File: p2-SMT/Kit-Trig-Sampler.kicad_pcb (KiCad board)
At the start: 2 copper layers, 78 x 109.2 mm, 81 parts, among them J1 START_CV, J10 AUDIO_INR, J11 AUDIO_OUTL, J13 BANK_CV, J14 Eurorack_Power_10pin_Unshroud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, J2 LENGTH_CV, J3 SAMP_CV, J4 PITCH CV, J5 REV_TRIG, J6 PLAY_TRIG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

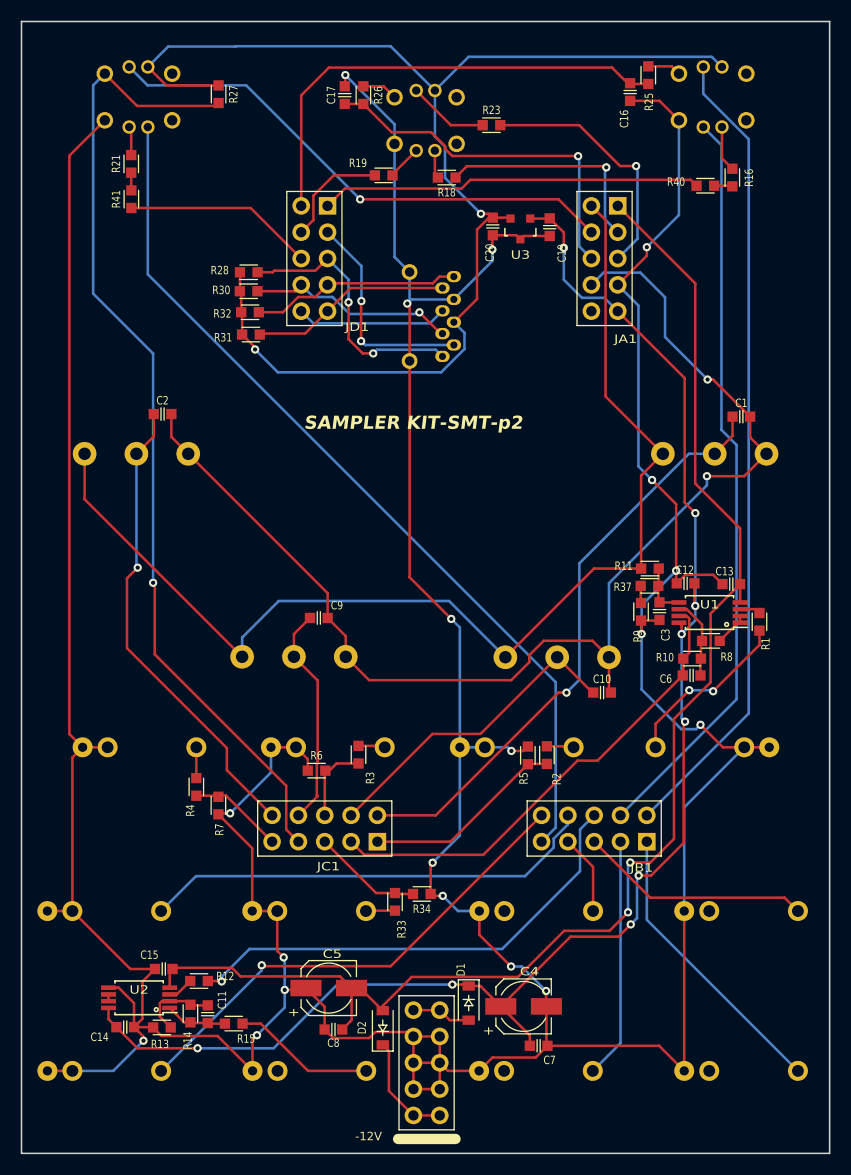
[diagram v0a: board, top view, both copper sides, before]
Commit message: Small tweeks to p2 smt  routing
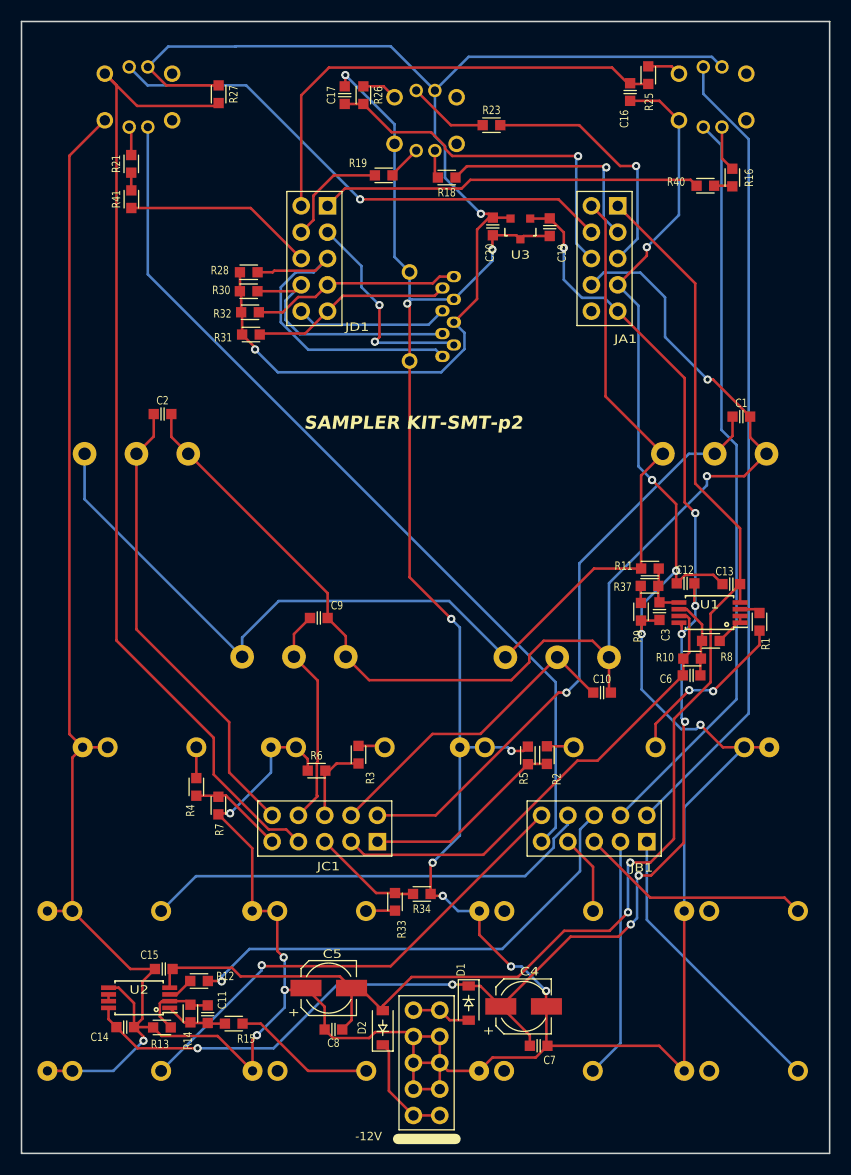
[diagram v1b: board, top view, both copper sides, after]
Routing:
- net /D18: track 26.0 -> 33.3 mm, vias 2 -> 0
- net /D4: track 20.0 -> 24.2 mm, vias 1 -> 0
- net /A9: track 45.7 -> 44.8 mm, vias 1 -> 0
- net /D19: track 21.0 -> 20.3 mm
- net /A6: vias 1 -> 0

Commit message: p2-SMT nudged traces to keep PWMs away from CV jacks
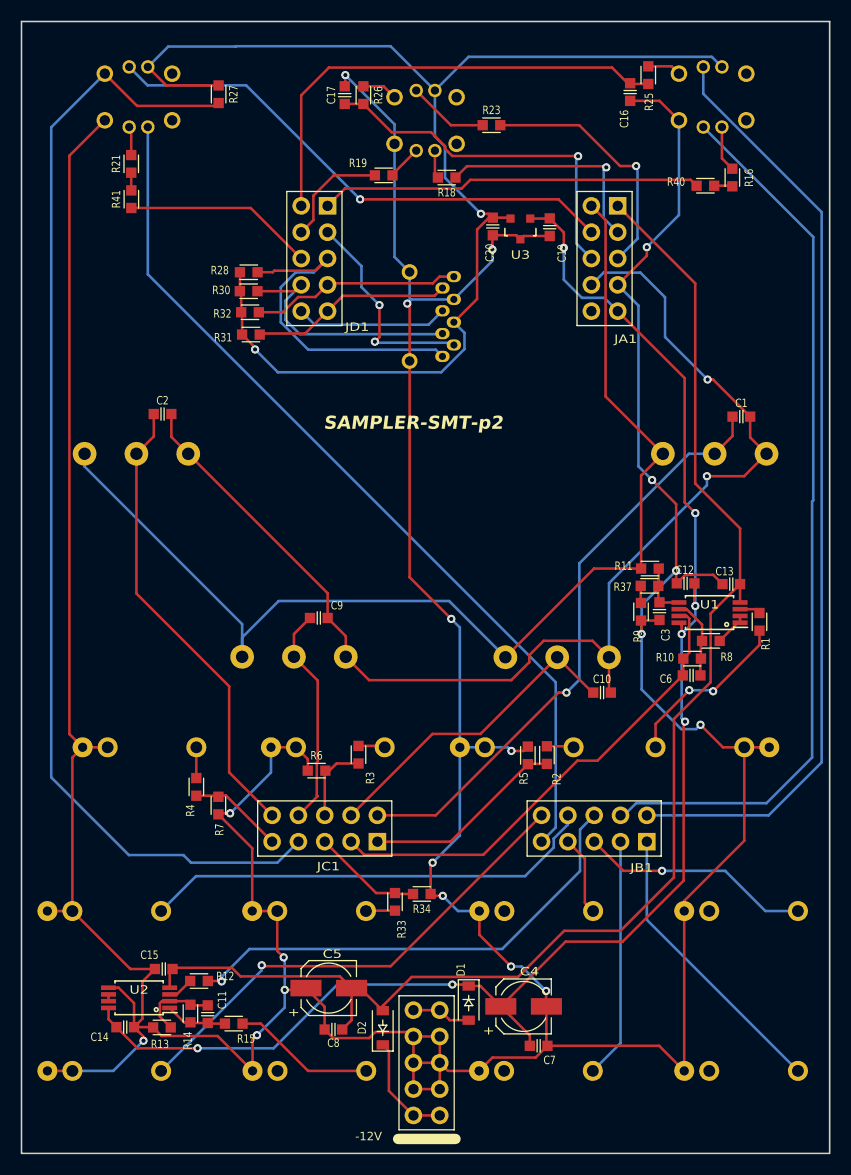
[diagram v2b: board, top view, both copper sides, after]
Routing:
- net /A6: track 95.3 -> 110.6 mm
- net /D1: track 72.4 -> 86.1 mm
- net /D0: track 78.1 -> 90.8 mm
- net -12VA: track 135.3 -> 134.7 mm, vias 2 -> 0
- net +12V: track 148.2 -> 148.0 mm, vias 9 -> 7
- net /AUDIO_IN2: vias 0 -> 1
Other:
- board text added: "SAMPLER-SMT-p2"
- board text removed: "SAMPLER KIT-SMT-p2"

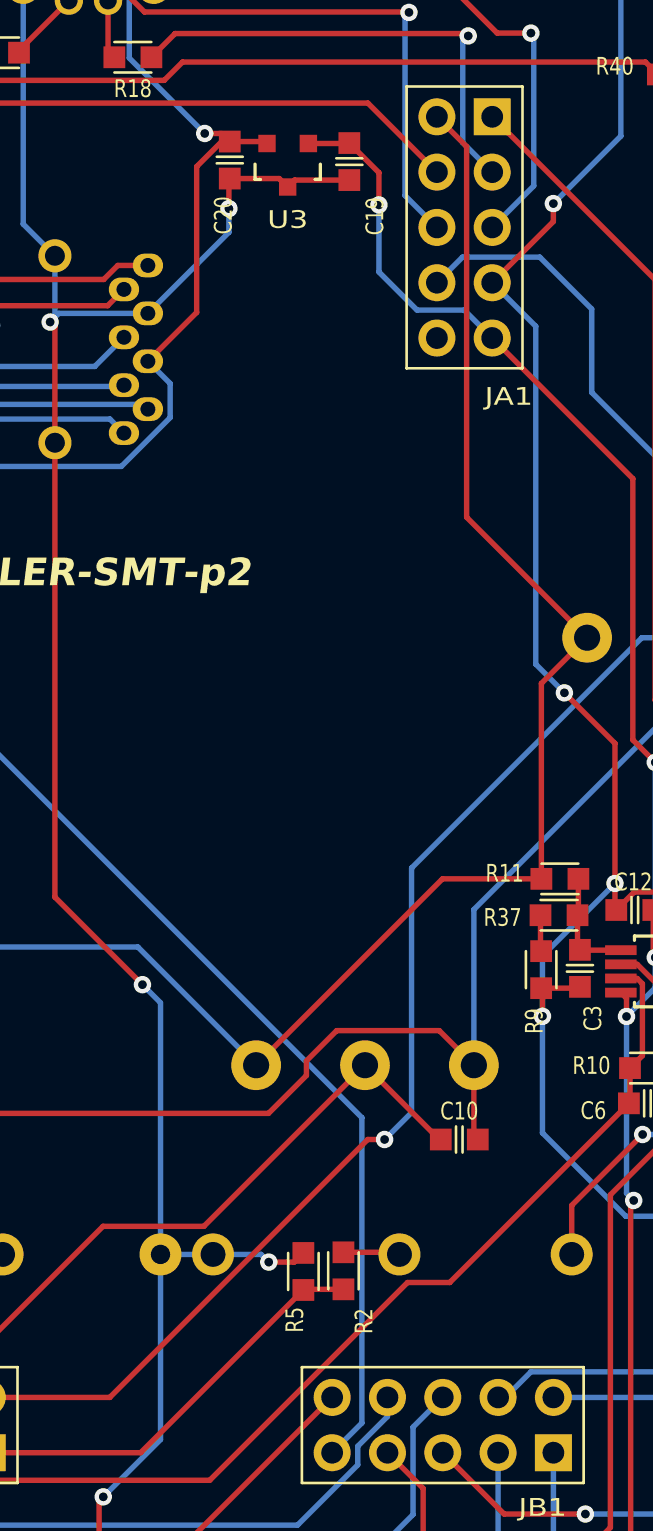
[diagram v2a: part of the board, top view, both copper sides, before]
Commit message: p2 SMT: swapped out U3 for different regulator
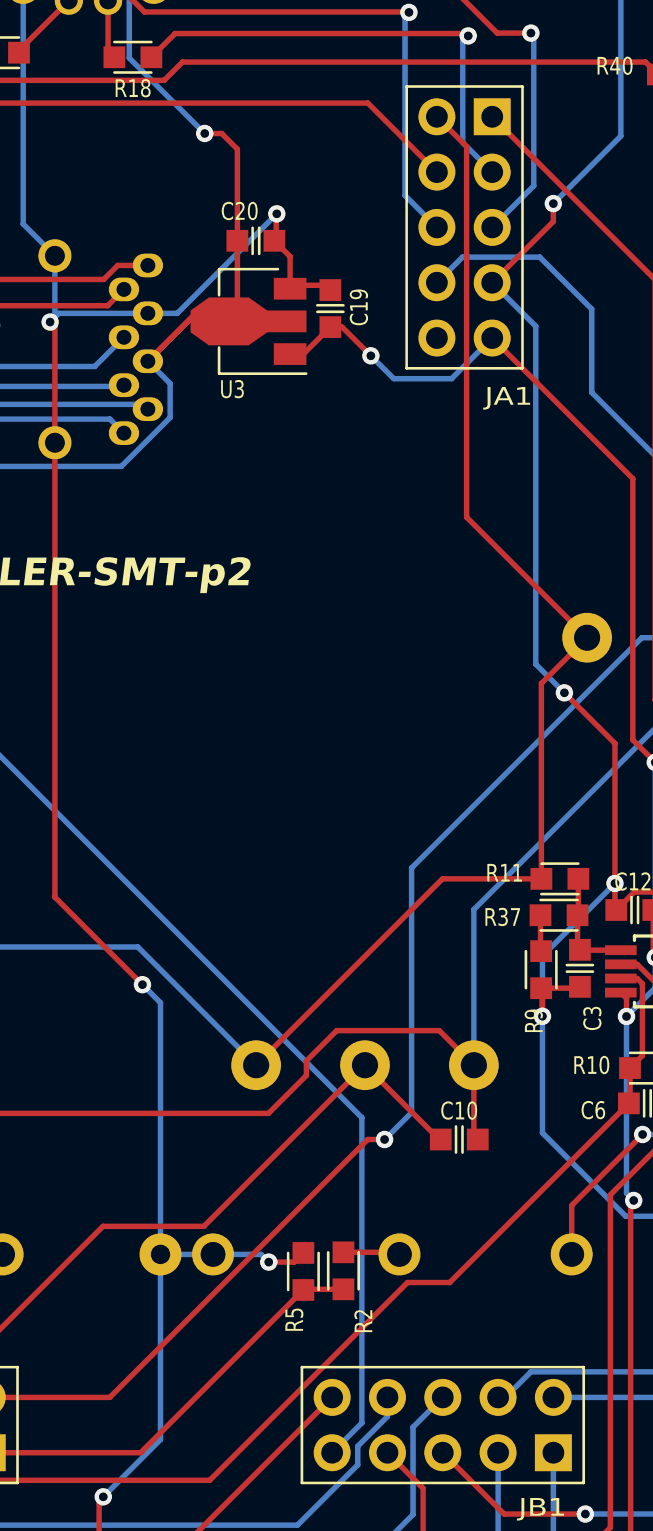
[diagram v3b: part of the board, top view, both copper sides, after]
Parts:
- U3: value AP7384-33 -> AZ1117CR-3.3TRG1; footprint 4ms_Package_SOT:SOT23-3_PO132 -> 4ms_Package_SOT:SOT89-3
- moved U3 7.30 mm to (58.8, 39.6)
- moved C19 6.81 mm to (62.1, 39.0), turned to 90 degrees
- moved C20 3.90 mm to (58.7, 35.9), turned to 0 degrees
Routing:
- net +12V: track 148.0 -> 144.1 mm
- net +3V3: track 127.7 -> 130.5 mm
- net GND: track 490.9 -> 490.4 mm
